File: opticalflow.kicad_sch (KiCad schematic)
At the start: 14 parts, among them U12 PMW3901MB-TXQT_C43496881, U14 LP5910-1.8DRVR

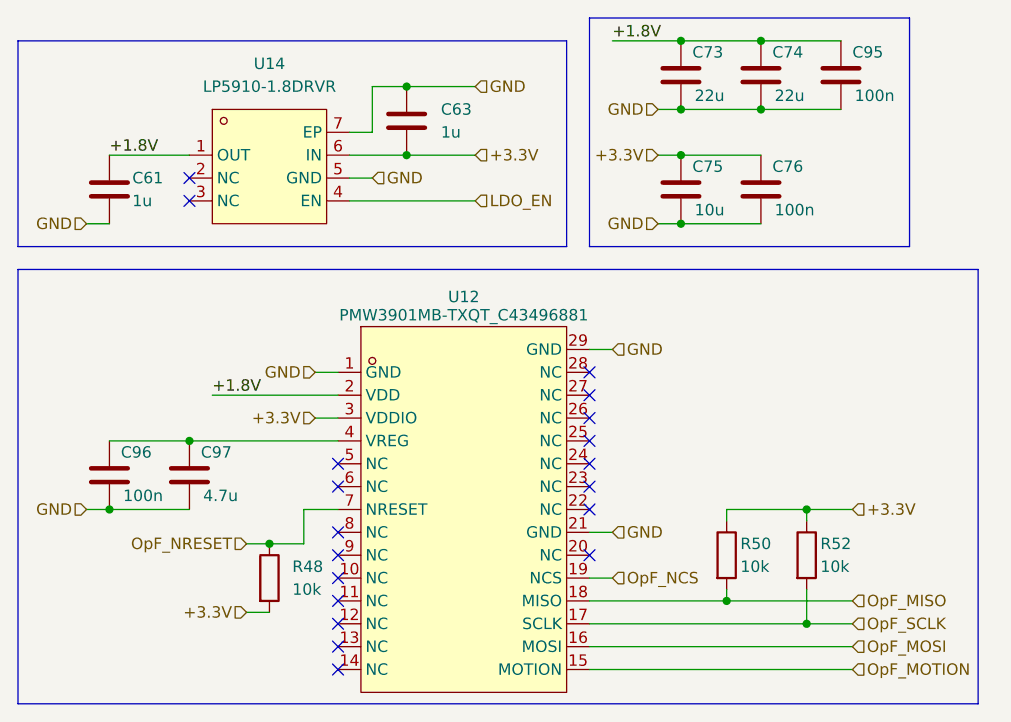
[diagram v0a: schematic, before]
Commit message: MCU Integration & Sensor Ports
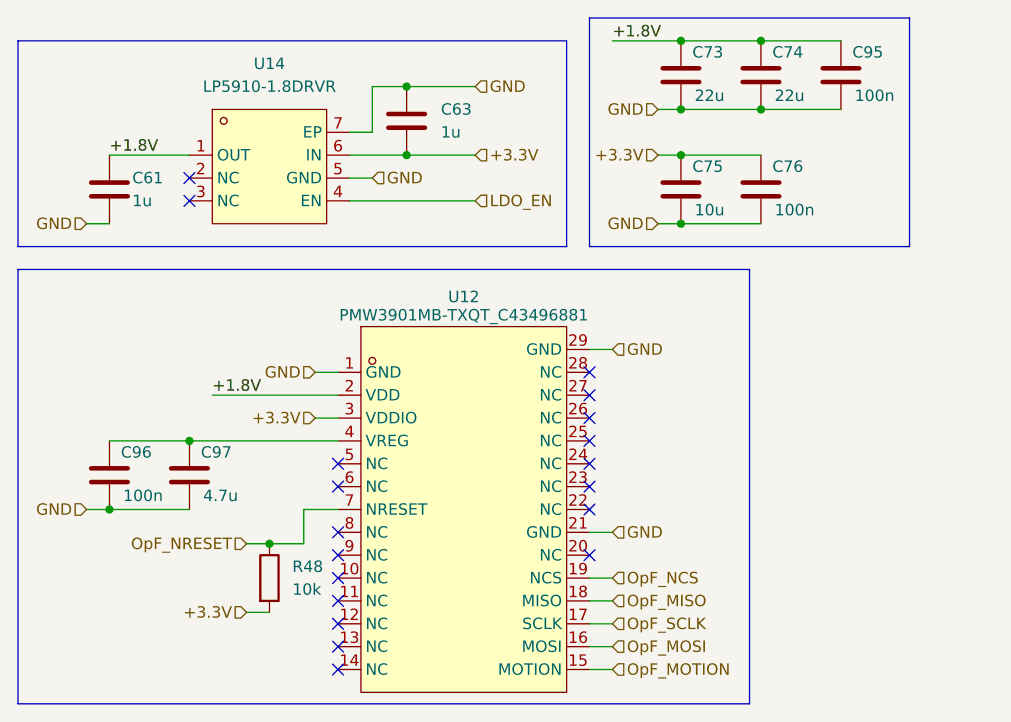
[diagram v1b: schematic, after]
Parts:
- removed R50, R52: 10k, symbol Device:R
